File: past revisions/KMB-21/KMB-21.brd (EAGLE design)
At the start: 90.2 x 95.9 mm, 141 parts, among them J1 503182-1852, J2 10118194-0001LF, J3 DCJ0303, Q1 IRLML2803, Q10 IRLML5103, Q11 IRLML5103, Q12 IRLML5103, Q13 IRLML5103, Q14 IRLML2803, Q15 IRLML2803, Q16 IRLML5103, Q2 IRLML2803, Q5 IRLML2803, Q6 IRLML2803, Q7 IRLML2803, Q8 IRLML2803, Q9 IRLML5103, U1 MAX706R, U12 EP2W+, U13 RFM23BP, U14 S1216V8, U15 XTB_2018_07_15, U16 XTB_2018_07_15, U17 XTB_2018_07_15, U18 XTB_2018_07_15, U2 FXAS21002FXAS21002, U20 MR25H40MDF, U3 LSM9DS1, U4 ATSAMD21G-A, U5 MAX4372TEUK+T, U6 LTC4121-4.2, U7 TPS54226PWPRPWP14_2P31X2P46-L, U8 PE014006, U9 PE014006, X1 BU-SMA-V, X2 BU-SMA-V, X3 BU-SMA-V, Y1 32.768kHz

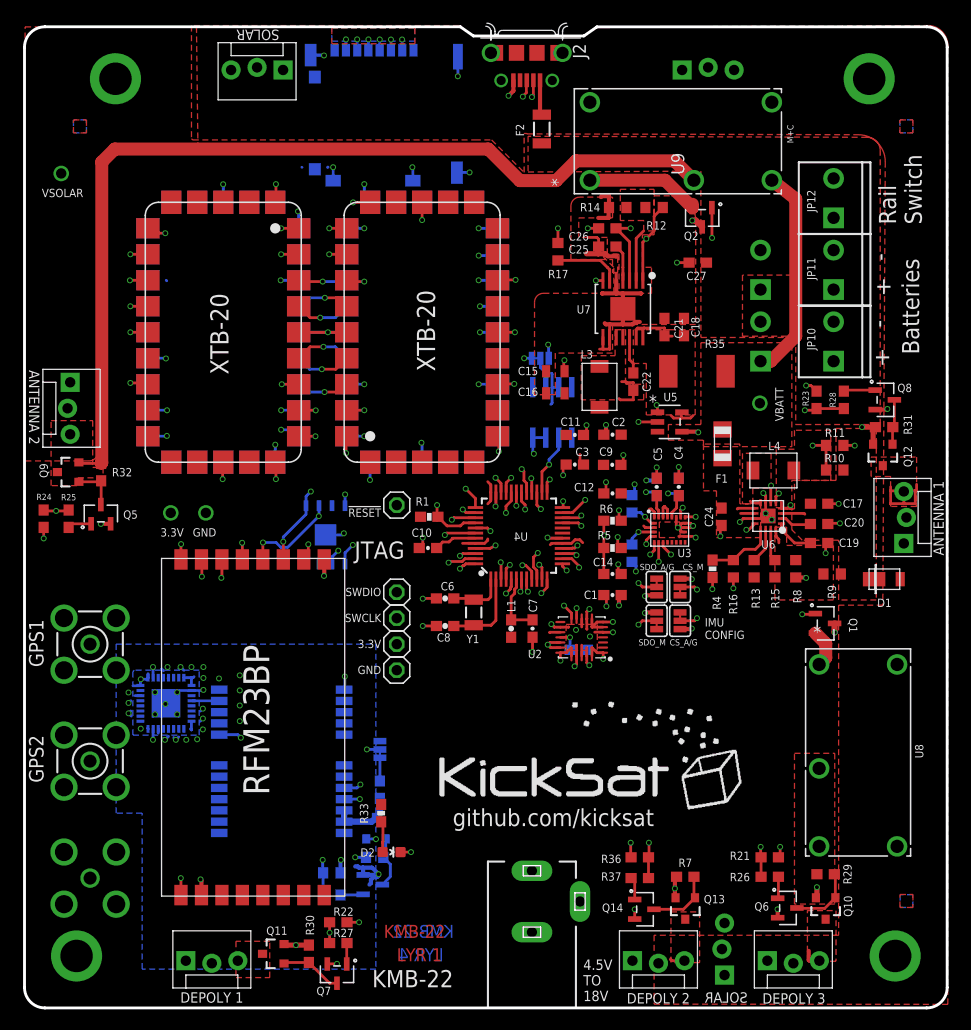
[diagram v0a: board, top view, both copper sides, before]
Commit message: added KMB-22 design
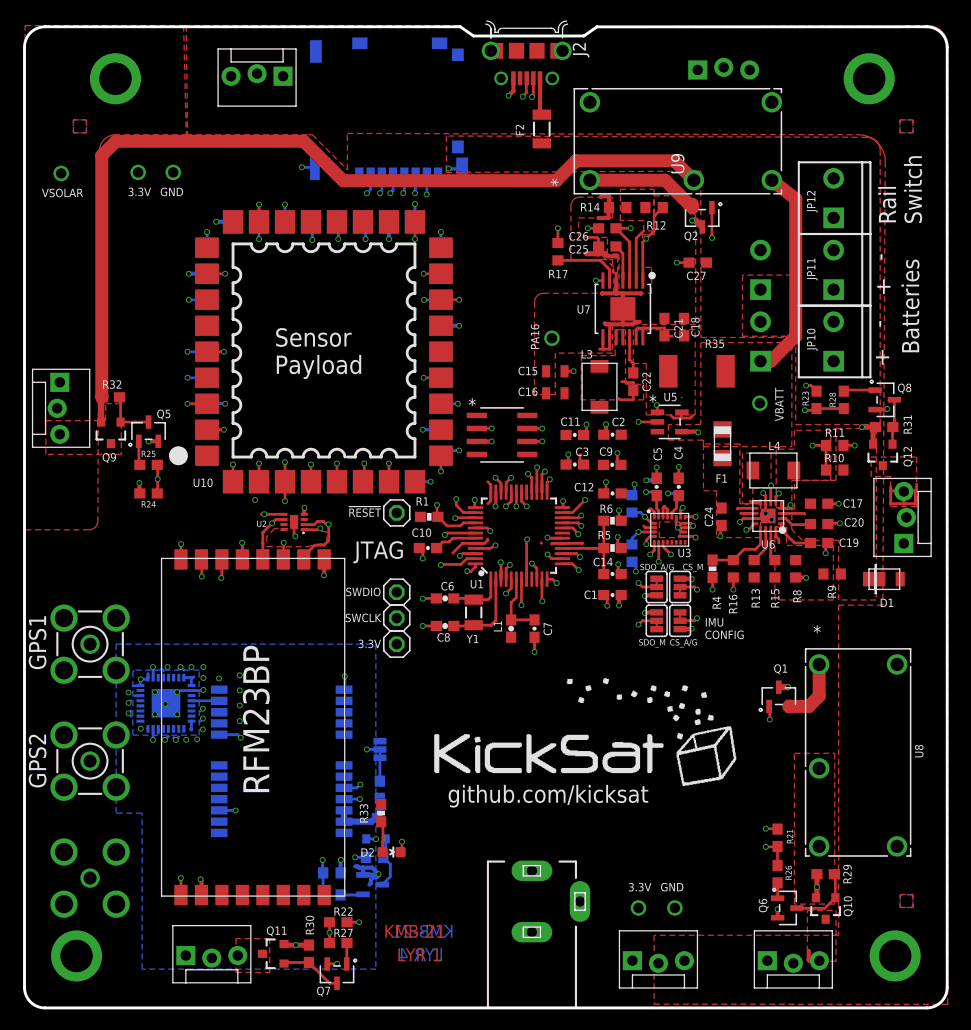
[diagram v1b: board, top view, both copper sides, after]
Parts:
- removed C28: 0.1uF, SparkFun-Capacitors:0603-CAP
- removed FRAME5: FRAME-LETTER, SparkFun-Aesthetics:CREATIVE_COMMONS
- removed GND: (no value), pinhead:1X01
- removed JP18: (no value), SparkFun-Passives:PAD-JUMPER-3-2OF3_NC_BY_TRACE_YES_SILK_FULL_BOX
- removed JP7: (no value), SparkFun-Connectors:MOLEX-1X3_LOCK
- removed Q13: IRLML5103, User-Submitted:SOT23-3
- removed Q14: IRLML2803, maholli:SOT-23
- removed R36: 10k, SparkFun-Resistors:0603
- removed R37: 4.7k, SparkFun-Resistors:0603
- removed R7: 100k, SparkFun-Resistors:0603
- removed U15, U16, U17, U18: XTB_2018_07_15, maholli:XTB28_MEZ
- removed U20: MR25H40MDF, maholli:SON127P600X500X90-9N
- added U10, U11: XTB_2018_04_25, maholli:XTB_MEZ
- U2: value FXAS21002FXAS21002 -> MR25H40; device maholli:QFN50P456X400X100-24 -> maholli:DFN-8
- moved U2 30.3 mm to (26.3, 47.5), turned to 90 degrees
- moved R24 10.5 mm to (12.1, 50.3), turned to 180 degrees
- moved R25 9.42 mm to (12.1, 53.1), turned to 0 degrees
- moved Q5 9.31 mm to (12.1, 56.4)
- moved JP14 8.96 mm to (59.4, 4.50), flipped to the top, turned to 0 degrees
- moved Q1 8.45 mm to (73.7, 30.5), turned to 0 degrees
- moved R32 7.38 mm to (8.38, 59.7), turned to 180 degrees
- moved Q9 5.67 mm to (8.38, 56.3), turned to 180 degrees
- moved U1 5.38 mm to (46.6, 56.0), flipped to the top, turned to 0 degrees
- moved L2 2.34 mm to (39.5, 21.5)
- moved L5 2.34 mm to (69.6, 21.1)
- moved R21 2.05 mm to (73.5, 16.6), turned to 90 degrees
- moved JP15 1.52 mm to (65.7, 91.8)
- moved JP6 1.01 mm to (3.27, 61.2)
- moved J1 0.81 mm to (35.6, 87.9), turned to 180 degrees
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- renumbered Q15 to Q3, Q16 to Q4
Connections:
- removed net ENAB_BURN5: R36.1, R37.2, U4.15
- removed net N$56: Q13.1, Q14.3, R7.1
- removed net N$57: Q14.1, R37.1
- removed net SPI_CS_XTB3: U17.P$7, U4.25
- removed net SPI_CS_XTB4: U18.P$7, U4.28
- removed net VBURN5: JP7.3, Q13.3
- new net GPS_1PPS: U14.3, U4.7
- new net LED_1: D2.C, U4.12
- new net N$31: U2.P$3
- new net N$49: U2.P$7
- new net N$54: U4.25
- new net N$55: U4.19
- new net WDT_PWR: U1.2
- new net XTB_START: U10.P$33, U11.P$33, U4.47
- net !RESET: no longer U1.8
- net 3.3V: now also U10.P$1, U10.P$18, U10.P$20, U10.P$24, U10.P$27, U10.P$3, U10.P$6, U10.P$7, U11.P$1, U11.P$18, U11.P$20, U11.P$24, U11.P$27, U11.P$3, U11.P$6, U11.P$7; no longer JP18.3, U15.P$1, U15.P$20, U15.P$22, U15.P$28, U16.P$1, U16.P$20, U16.P$22, U16.P$28, U17.P$1, U17.P$20, U17.P$22, U17.P$28, U18.P$1, U18.P$20, U18.P$22, U18.P$28, U2.15, U2.17, U2.18, U20.8
- net BURN_RELAY_B: now also U4.15; no longer U4.27
- net ENAB_BURN1: now also U4.48; no longer U4.47
- net ENAB_BURN4: now also U4.13; no longer U4.16
- net ENAB_GPS: now also U4.11; no longer U4.12
- net GND: now also U10.P$11, U10.P$17, U10.P$19, U10.P$2, U10.P$23, U10.P$28, U10.P$34, U10.P$5, U10.P$8, U11.P$11, U11.P$17, U11.P$19, U11.P$2, U11.P$23, U11.P$28, U11.P$34, U11.P$5, U11.P$8, U2.P$4, U2.P$9; no longer C28.1, GND.1, JP18.1, JP7.1, Q14.2, R36.2, U1.4, U15.P$10, U15.P$12, U15.P$17, U15.P$19, U15.P$2, U15.P$21, U15.P$23, U15.P$8, U15.P$9, U16.P$10, U16.P$12, U16.P$17, U16.P$19, U16.P$2, U16.P$21, U16.P$23, U16.P$8, U16.P$9, U17.P$10, U17.P$12, U17.P$17, U17.P$19, U17.P$2, U17.P$21, U17.P$23, U17.P$8, U17.P$9, U18.P$10, U18.P$12, U18.P$17, U18.P$19, U18.P$2, U18.P$21, U18.P$23, U18.P$8, U18.P$9, U2.1, U2.10, U2.14, U2.19, U2.20, U2.21, U2.22, U2.23, U2.24, U2.5, U2.6, U2.7, U2.8, U2.9, U20.4, U20.9
- net I2C_SCL: no longer U2.11
- net I2C_SDA: no longer U2.12
- net I_BATT: now also U4.10; no longer U4.9
- net N$13: now also U4.16; no longer U4.10
- net N$22: now also U4.9; no longer C28.2, U2.16
- net N$39: now also U2.P$8; no longer R4.2, U4.11
- net N$53: now also U4.29; no longer D2.C, U4.13
- net N$8: now also R4.2, U4.20; no longer JP18.2, U1.2
- net SPI_CS_MRAM: now also U2.P$1; no longer U20.1, U4.38
- net SPI_CS_RFM: now also U4.41; no longer U4.48
- net SPI_CS_SD: now also U4.38; no longer U4.29
- net SPI_CS_XTB1: now also U10.P$32, U4.39; no longer U15.P$7, U4.41
- net SPI_CS_XTB2: now also U11.P$32, U4.8; no longer U16.P$7, U4.37
- net SPI_MISO: now also U10.P$29, U11.P$29, U2.P$2, U4.31; no longer U15.P$4, U16.P$4, U17.P$4, U18.P$4, U20.2, U4.30
- net SPI_MOSI: now also U10.P$31, U11.P$31, U2.P$5, U4.30; no longer U15.P$6, U16.P$6, U17.P$6, U18.P$6, U20.5, U4.31
- net SPI_SCK: now also U10.P$30, U11.P$30, U2.P$6; no longer U15.P$5, U16.P$5, U17.P$5, U18.P$5, U20.6
- net UART1_RX: now also U4.27; no longer U4.7
- net UART1_TX: now also U4.26; no longer U4.8
- net VBURN_B_IN: no longer Q13.2, R7.2
- net VSOLAR: no longer JP7.2, JP8.2
- net WDT_WDI: now also U4.28; no longer U4.26
- net XTB_RESET: now also U10.P$26, U11.P$26, U4.37; no longer U15.P$3, U16.P$3, U17.P$3, U18.P$3, U4.39
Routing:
- net SPI_CS_XTB3: track 62.0 -> 0.00 mm, vias 2 -> 0
- net XTB_START: track 0.00 -> 59.3 mm, vias 0 -> 3
- net GND: track 210.0 -> 156.8 mm, vias 140 -> 115
- net SPI_CS_XTB2: track 33.1 -> 77.9 mm
- net GPS_1PPS: track 0.00 -> 43.7 mm, vias 0 -> 2
- net N$53: track 36.9 -> 0.00 mm, vias 2 -> 0
- net ENAB_BURN5: track 36.6 -> 0.00 mm, vias 2 -> 0
- net LED_1: track 0.00 -> 34.0 mm, vias 0 -> 2
- net SPI_MISO: track 98.0 -> 72.6 mm, vias 6 -> 5
- net SPI_CS_XTB4: track 24.2 -> 0.00 mm, vias 2 -> 0
- net XTB_RESET: track 55.5 -> 31.7 mm
- net 3.3V: track 92.5 -> 69.0 mm, vias 27 -> 22
- net N$39: track 23.0 -> 0.00 mm, vias 2 -> 0
- net SPI_MOSI: track 99.1 -> 79.0 mm
- net I2C_SCL: track 29.2 -> 11.2 mm, vias 3 -> 2
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- removed copper zone on layer 1, net VBURN5
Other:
- board text added: "KMB-21"
- board text added: "PA16"
- board text added: "Sensor Payload"
- board text removed: "4.5V TO 18V"
- board text removed: "ANTENNA 1"
- board text removed: "ANTENNA 2"
- board text removed: "DEPOLY 1"
- board text removed: "DEPOLY 2"
- board text removed: "DEPOLY 3"
- board text removed: "KMB-22"
- board text removed: "M+C"
- board text removed: "SOLAR"
